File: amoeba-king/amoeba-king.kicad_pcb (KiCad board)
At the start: 2 copper layers, 19 x 19.1 mm, 14 parts, among them J1 Conn_01x04_Male, J2 Conn_01x04_Male, J3 Conn_01x04_Male, J4 Conn_01x04_Male, J5 Conn_01x01_Male, J6 Conn_01x01_Male

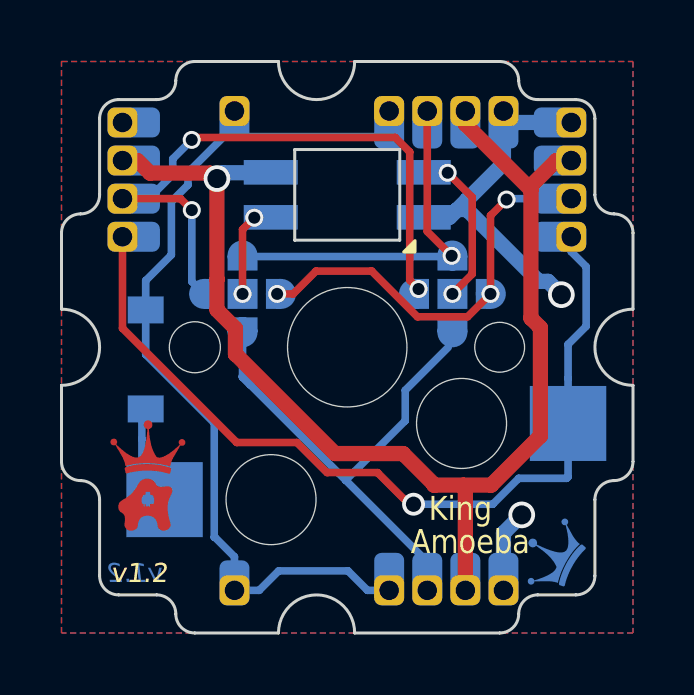
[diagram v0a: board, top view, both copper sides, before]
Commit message: Migrate Amoeba King to KiCad 10, bundle 3D models, and fix DRC/ERC
- Convert schematics and PCB to KiCad 10 format
- Add bundled local 3D models with relative ${KIPRJMOD} paths (Switch, Kailh socket, DSA keycap, SK6812 MINI-E, SOD-123 diode)
- Bundle and reference all symbols and footprints locally in amoeba-modules
- Fix dangling track, missing junctions, and net connections
- Configure board and schematic design rules for 0 DRC and 0 ERC violations
- Update Makefile for kicad-cli DRC, ERC, and Gerber export
- Remove obsolete legacy KiCad 4/5 files
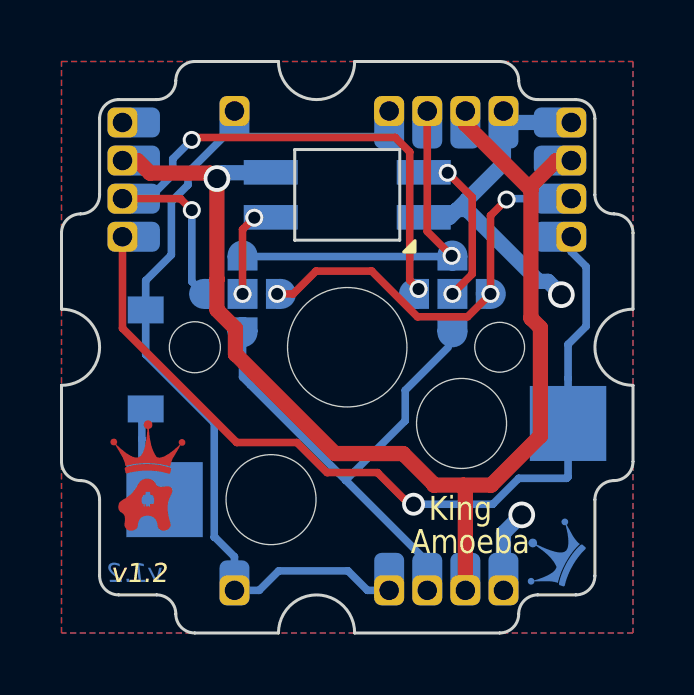
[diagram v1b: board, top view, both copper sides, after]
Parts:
- D1: footprint Diode_SMD:D_SOD-123 -> amoeba-modules:D_SOD-123
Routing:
- net Net-(J4-Pad2): track 18.6 -> 17.3 mm
